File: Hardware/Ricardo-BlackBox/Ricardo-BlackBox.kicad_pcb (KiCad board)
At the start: 4 copper layers, 45.1 x 35.1 mm, 83 parts, among them J1 RBUS, J2 USB_C_Receptacle_USB2.0, J3 Conn_02x04_Odd_Even, U1 ESP32-S3, U2 SN65HVD230, U3 LM66200DRLR, U4 MAX77827AEFD+T, U5 SC4215ASTRT, U6 XTSD08G, U7 LM66200DRLR, Y1 R940000171

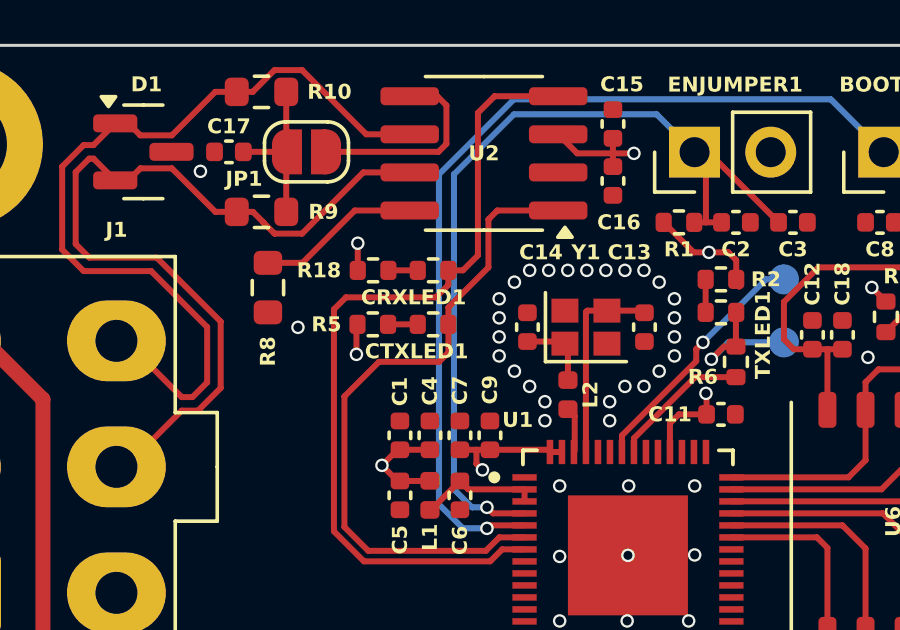
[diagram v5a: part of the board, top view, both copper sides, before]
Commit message: Update crystal exclusion zone and grounding
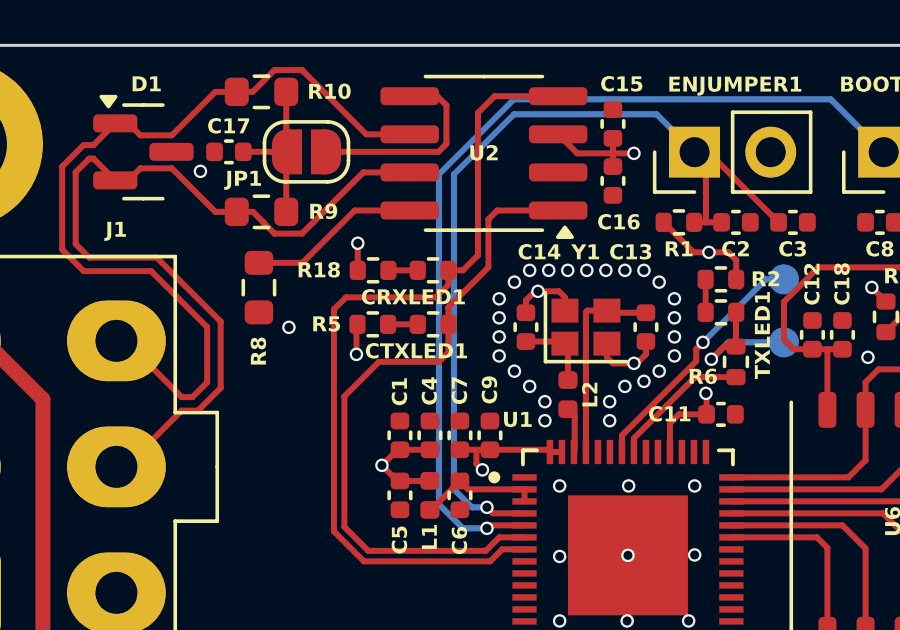
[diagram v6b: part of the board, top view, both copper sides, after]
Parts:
- moved R8 0.30 mm to (92.4, 53.9)
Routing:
- net GND: track 9.34 -> 14.1 mm, vias 50 -> 52

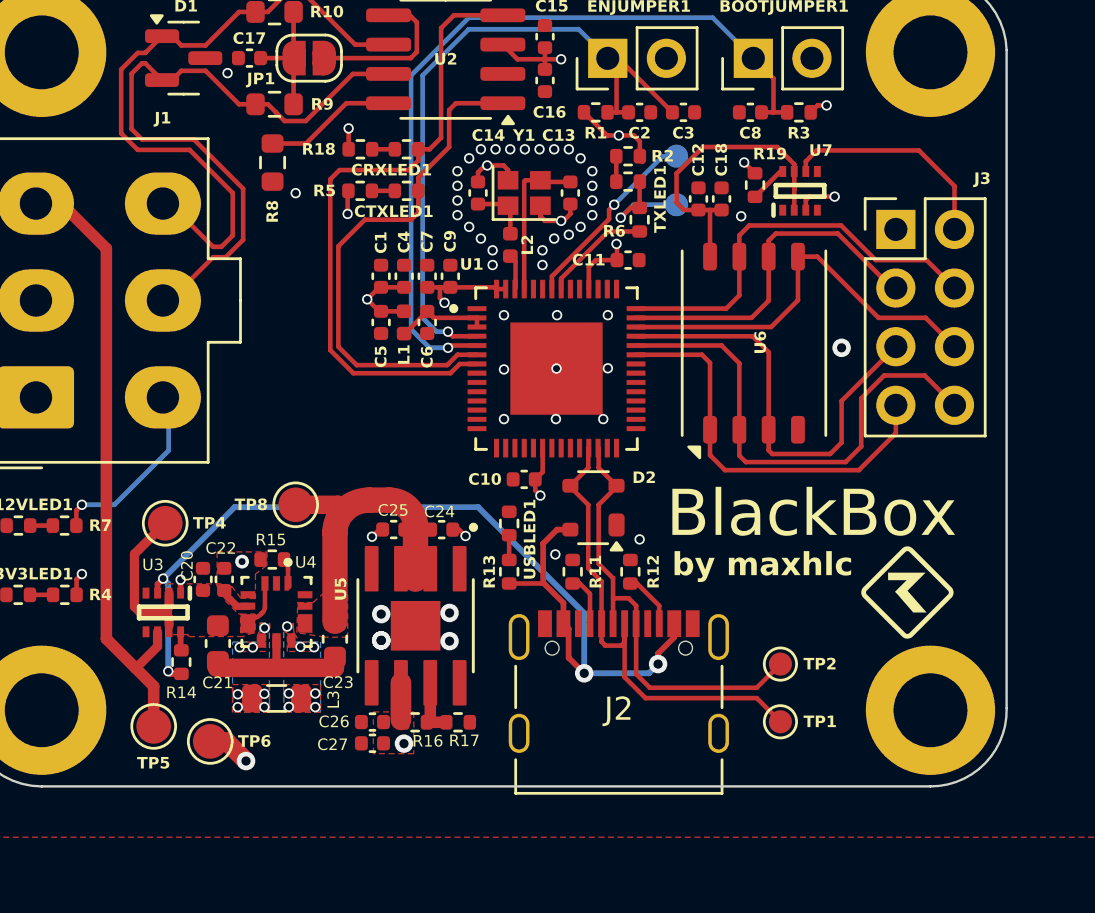
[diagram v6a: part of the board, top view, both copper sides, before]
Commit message: Changed NAND flash to ZDSD04GLGEAG
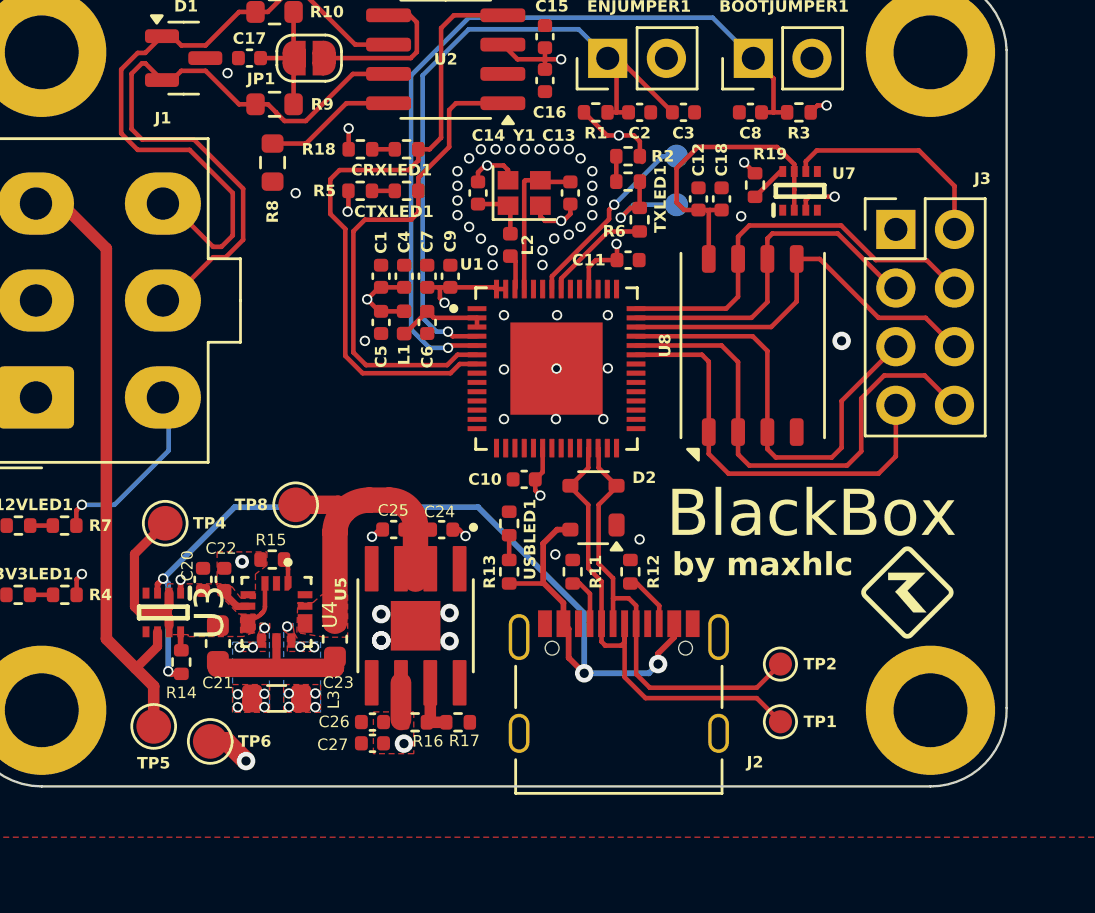
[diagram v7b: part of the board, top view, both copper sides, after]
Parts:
- removed U6: XTSD08G, Package_LGA:LGA-8_8x6mm_P1.27mm
- added U8: ~, Package_LGA:LGA-8_8x6mm_P1.27mm, F.Cu at (113.2, 61.8)
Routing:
- net /CAN_TX: track 22.4 -> 21.6 mm
- net /NAND_SD2: track 17.5 -> 18.3 mm
- net GND: vias 52 -> 53

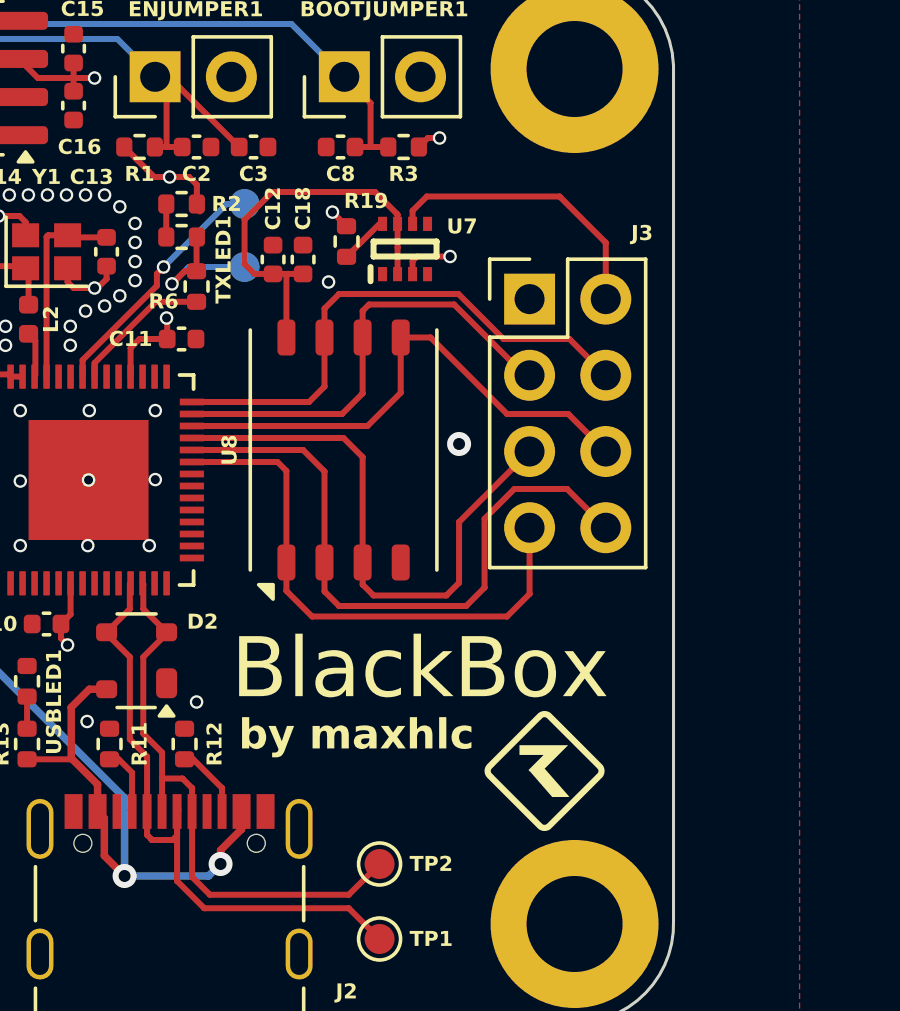
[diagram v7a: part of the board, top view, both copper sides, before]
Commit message: Switched to PicoBlade connector
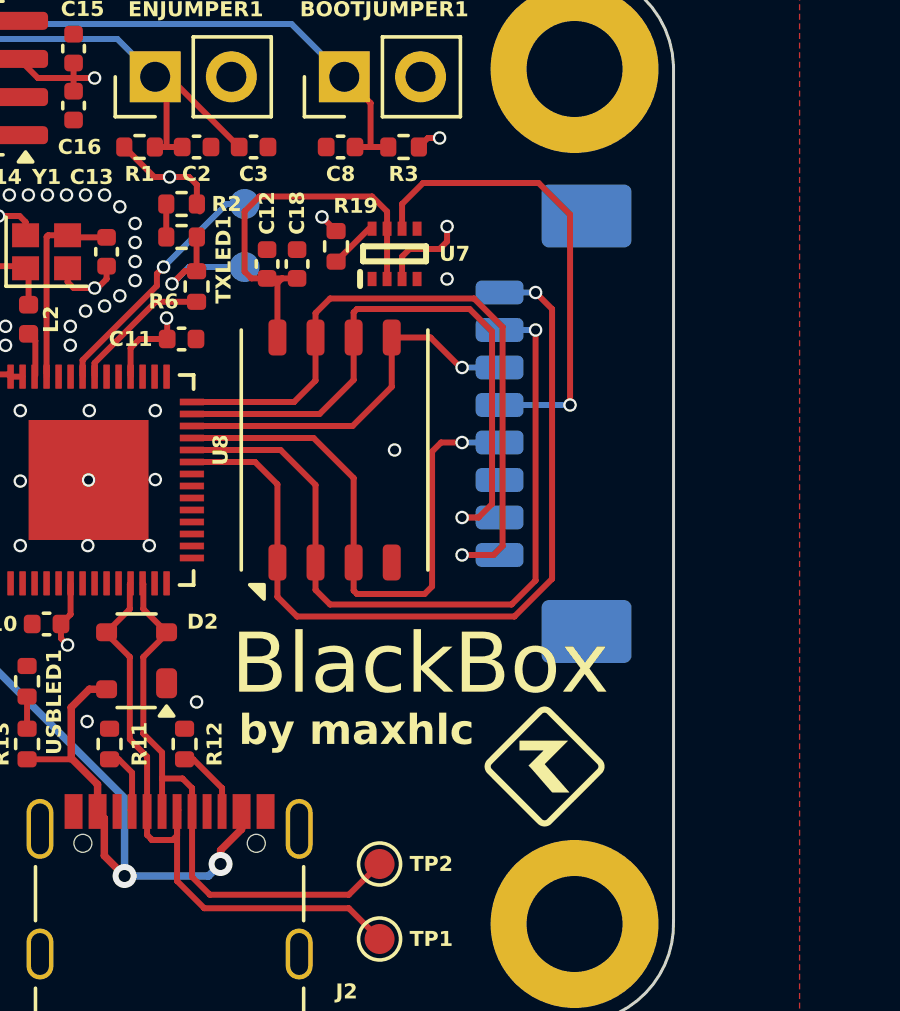
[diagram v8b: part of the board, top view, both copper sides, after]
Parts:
- J3: value Conn_02x04_Odd_Even -> Conn_01x08_Pin; footprint Connector_PinHeader_2.54mm:PinHeader_2x04_P2.54mm_Vertical -> Connector_Molex:Molex_PicoBlade_53261-0871_1x08-1MP_P1.25mm_Horizontal; moved to B.Cu
- moved J3 4.38 mm to (120.8, 60.9), turned to -90 degrees
- moved R19 0.39 mm to (113.0, 55.0)
- moved U7 0.39 mm to (114.9, 55.3)
- moved U8 0.30 mm to (112.9, 61.8)
- moved C12 0.25 mm to (110.7, 55.6)
- moved C18 0.25 mm to (111.7, 55.6)
- moved G*** 0.15 mm to (119.9, 72.3)
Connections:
- J3 pad 1: GND -> /NAND_SD2
- J3 pad 2: /HEADER_3V3 -> /NAND_SD3
- J3 pad 3: /NAND_SD0 -> /NAND_CMD
- J3 pad 4: /NAND_SD1 -> /HEADER_3V3
- J3 pad 6: /NAND_CMD -> GND
- J3 pad 7: /NAND_SD2 -> /NAND_SD0
- J3 pad 8: /NAND_SD3 -> /NAND_SD1
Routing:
- net /NAND_SD2: track 18.3 -> 27.8 mm, vias 0 -> 1
- net /HEADER_3V3: track 9.59 -> 15.8 mm, vias 0 -> 1
- net /NAND_SD0: track 15.4 -> 21.3 mm, vias 0 -> 1
- net /NAND_SD1: track 17.9 -> 23.5 mm, vias 0 -> 1
- net /NAND_CMD: track 17.7 -> 12.9 mm, vias 0 -> 1
- net /NAND_SD3: track 21.8 -> 25.5 mm, vias 0 -> 1
- net +3V3: track 30.2 -> 31.4 mm
- net /NAND_CLK: track 19.2 -> 19.3 mm, vias 0 -> 1
